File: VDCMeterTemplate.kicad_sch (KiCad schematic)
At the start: 14 parts

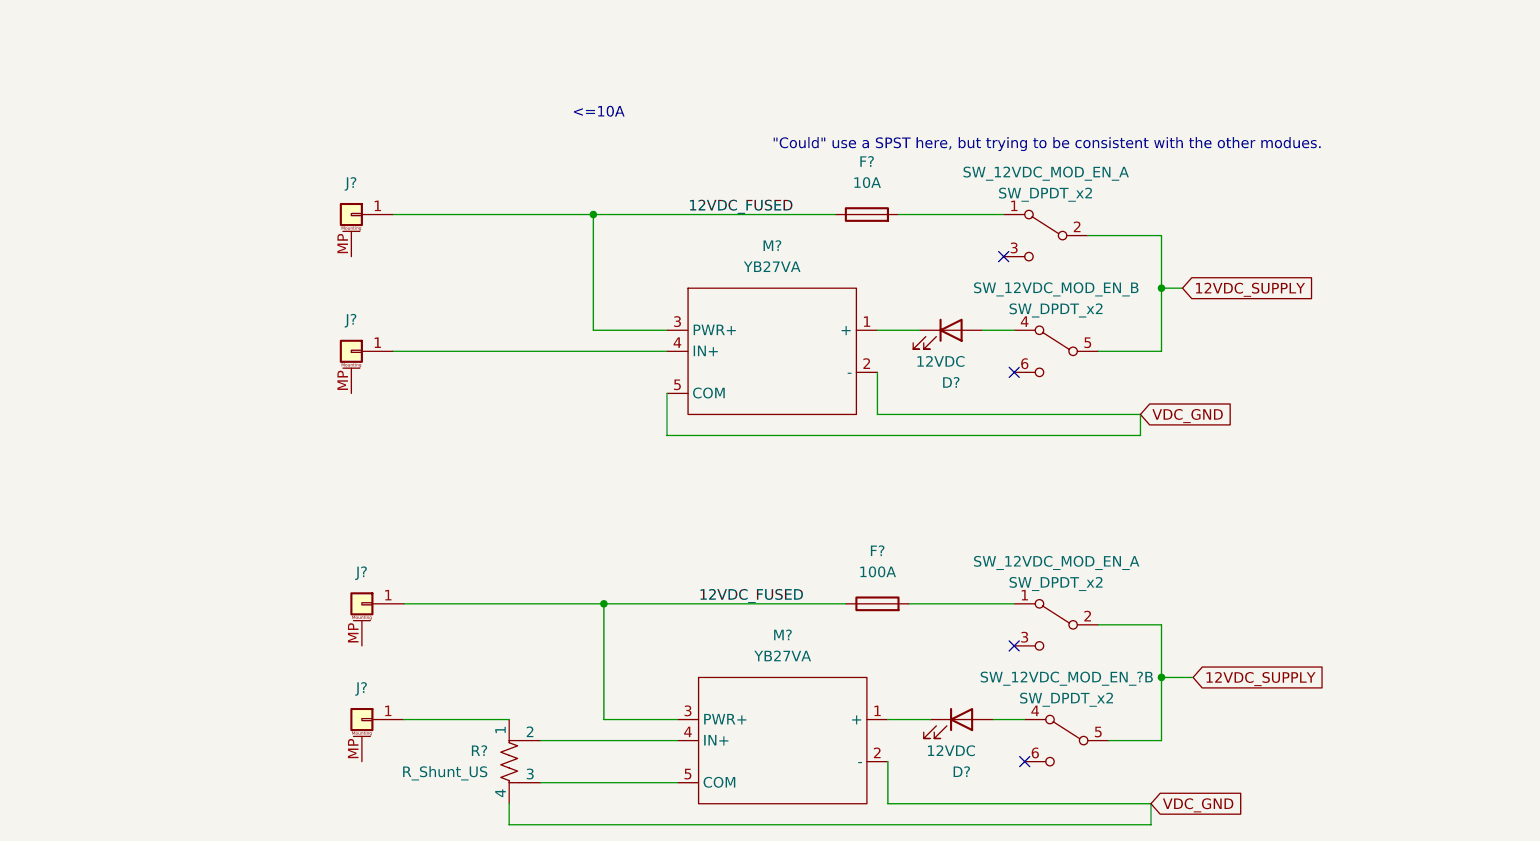
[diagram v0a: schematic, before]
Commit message: Save more changes
Started Fan Control
Created VDC Meter Template
Fleshed out 12, 5, 5-usb, and 3.3 modules
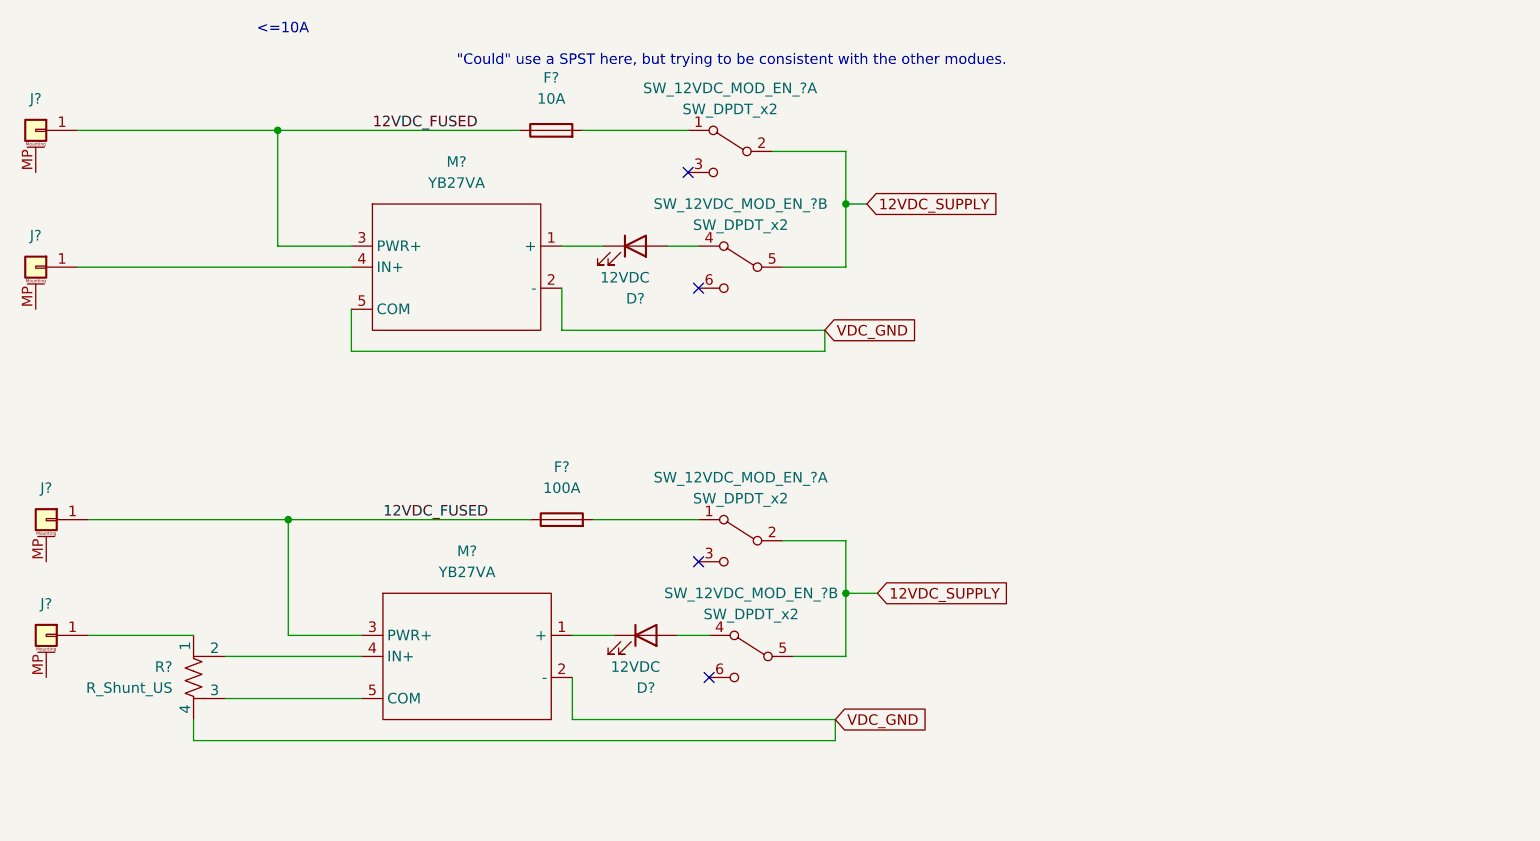
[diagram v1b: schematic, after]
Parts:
- removed D? (x2): 12VDC, symbol Device:LED
- removed F?: 10A, symbol Device:Fuse
- removed F?: 100A, symbol Device:Fuse
- removed J? (x4): Conn_01x01_MountingPin, symbol Connector_Generic_MountingPin:Conn_01x01_MountingPin
- removed M? (x2): YB27VA, symbol bvm-library:5_Pin_Meter_With_Ext_Shunt
- removed R?: R_Shunt_US, symbol Device:R_Shunt_US
- removed SW_12VDC_MOD_EN_ (x2), SW_12VDC_MOD_EN_?: SW_DPDT_x2, symbol Switch:SW_DPDT_x2
- added D? (x2): 12VDC, symbol Device:LED
- added F?: 10A, symbol Device:Fuse
- added F?: 100A, symbol Device:Fuse
- added J? (x4): Conn_01x01_MountingPin, symbol Connector_Generic_MountingPin:Conn_01x01_MountingPin
- added M? (x2): YB27VA, symbol bvm-library:5_Pin_Meter_With_Ext_Shunt
- added R?: R_Shunt_US, symbol Device:R_Shunt_US
- added SW_12VDC_MOD_EN_? (x4): SW_DPDT_x2, symbol Switch:SW_DPDT_x2
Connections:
- net 12VDC_FUSED: now also F?.1, F?.1, J?.1 (Pin_1), J?.1 (Pin_1), M?.3 (PWR+), M?.3 (PWR+)
- net 12VDC_SUPPLY: now also SW_12VDC_MOD_EN_?.2 (B), SW_12VDC_MOD_EN_?.2 (B), SW_12VDC_MOD_EN_?.5 (B), SW_12VDC_MOD_EN_?.5 (B)
- net VDC_GND: now also M?.2 (-), M?.2 (-), M?.5 (COM), R?.4
- new net: F?.2, SW_12VDC_MOD_EN_?.1 (A) (x2)
- new net: J?.1 (Pin_1), R?.1
- new net: M?.4 (IN+), R?.2
- new net: M?.5 (COM), R?.3
- new net: D?.1 (K), M?.1 (+) (x2)
- new net: J?.1 (Pin_1), M?.4 (IN+)
- new net: D?.2 (A), SW_12VDC_MOD_EN_?.4 (A) (x2)
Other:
- company: eatmellc -> (none)

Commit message: Bunch more changes
Blah blah
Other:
- note added: "< 10Amp Version"
- note added: ">= 10Amp Version"
- note added: "Can I make use of some kind of switch that would allow me to enable/disable the shunt?"
- note removed: "<=10A"
- company: (none) -> eatmellc
- title: (none) -> Mr. Powers
- moved on the sheet: D?, F?, J?, M?, SW_12VDC_MOD_EN_?A, SW_12VDC_MOD_EN_?B

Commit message: Minor change across the board
I need better notes.
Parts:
- gave numbers to parts that had none: 13
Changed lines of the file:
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@@
   (symbol (lib_id "Device:Fuse") (at 173.99 38.1 90) (unit 1)
     (in_bom yes) (on_board yes) (fields_autoplaced)
-    (property "Reference" "F?" (id 0) (at 173.99 31.75 90))
+    (property "Reference" "F7" (id 0) (at 173.99 31.75 90))
     (property "Value" "10A" (id 1) (at 173.99 34.29 90))
     (property "Footprint" "" (id 2) (at 173.99 39.878 90)
@@
   (symbol (lib_id "Device:R_Shunt_US") (at 132.08 127 0) (unit 1)
     (in_bom yes) (on_board yes) (fields_autoplaced)
-    (property "Reference" "R?" (id 0) (at 129.54 125.7299 0)
+    (property "Reference" "R5" (id 0) (at 129.54 125.7299 0)
       (effects (font (size 1.27 1.27)) (justify right))
     )
@@
   (symbol (lib_id "Switch:SW_DPDT_x2") (at 198.12 110.49 0) (mirror y) (unit 1)
     (in_bom yes) (on_board yes) (fields_autoplaced)
-    (property "Reference" "SW_12VDC_MOD_EN_?" (id 0) (at 198.12 102.87 0))
+    (property "Reference" "SW_12VDC_MOD_EN_3" (id 0) (at 198.12 102.87 0))
     (property "Value" "SW_DPDT_x2" (id 1) (at 198.12 105.41 0))
     (property "Footprint" "" (id 2) (at 198.12 110.49 0)
@@
   (symbol (lib_id "Connector_Generic_MountingPin:Conn_01x01_MountingPin") (at 114.3 121.92 0) (mirror y) (unit 1)
     (in_bom yes) (on_board yes) (fields_autoplaced)
-    (property "Reference" "J?" (id 0) (at 114.3 118.11 0))
+    (property "Reference" "J19" (id 0) (at 114.3 118.11 0))
     (property "Value" "Conn_01x01_MountingPin" (id 1) (at 111.76 123.5455 0)
       (effects (font (size 1.27 1.27)) (justify left) hide)
@@
   (symbol (lib_id "bvm-library:5_Pin_Meter_With_Ext_Shunt") (at 160.02 127 0) (unit 1)
     (in_bom yes) (on_board yes) (fields_autoplaced)
-    (property "Reference" "M?" (id 0) (at 165.1 111.76 0))
+    (property "Reference" "M11" (id 0) (at 165.1 111.76 0))
     (property "Value" "YB27VA" (id 1) (at 165.1 114.3 0))
     (property "Footprint" "" (id 2) (at 160.02 127 0)
@@
   (symbol (lib_id "Connector_Generic_MountingPin:Conn_01x01_MountingPin") (at 111.76 54.61 0) (mirror y) (unit 1)
     (in_bom yes) (on_board yes) (fields_autoplaced)
-    (property "Reference" "J?" (id 0) (at 111.76 50.8 0))
+    (property "Reference" "J17" (id 0) (at 111.76 50.8 0))
     (property "Value" "Conn_01x01_MountingPin" (id 1) (at 109.22 56.2355 0)
       (effects (font (size 1.27 1.27)) (justify left) hide)
@@
   (symbol (lib_id "Device:LED") (at 184.15 52.07 0) (unit 1)
     (in_bom yes) (on_board yes)
-    (property "Reference" "D?" (id 0) (at 184.15 58.42 0))
+    (property "Reference" "D7" (id 0) (at 184.15 58.42 0))
     (property "Value" "12VDC" (id 1) (at 182.88 55.88 0))
     (property "Footprint" "" (id 2) (at 184.15 52.07 0)
@@
   (symbol (lib_id "Connector_Generic_MountingPin:Conn_01x01_MountingPin") (at 114.3 107.95 0) (mirror y) (unit 1)
     (in_bom yes) (on_board yes) (fields_autoplaced)
-    (property "Reference" "J?" (id 0) (at 114.3 104.14 0))
+    (property "Reference" "J18" (id 0) (at 114.3 104.14 0))
     (property "Value" "Conn_01x01_MountingPin" (id 1) (at 111.76 109.5755 0)
       (effects (font (size 1.27 1.27)) (justify left) hide)
@@
   (symbol (lib_id "bvm-library:5_Pin_Meter_With_Ext_Shunt") (at 157.48 57.15 0) (unit 1)
     (in_bom yes) (on_board yes) (fields_autoplaced)
-    (property "Reference" "M?" (id 0) (at 162.56 41.91 0))
+    (property "Reference" "M10" (id 0) (at 162.56 41.91 0))
     (property "Value" "YB27VA" (id 1) (at 162.56 44.45 0))
     (property "Footprint" "" (id 2) (at 157.48 57.15 0)
@@
   (symbol (lib_id "Device:Fuse") (at 176.53 107.95 90) (unit 1)
     (in_bom yes) (on_board yes) (fields_autoplaced)
-    (property "Reference" "F?" (id 0) (at 176.53 101.6 90))
+    (property "Reference" "F8" (id 0) (at 176.53 101.6 90))
     (property "Value" "100A" (id 1) (at 176.53 104.14 90))
     (property "Footprint" "" (id 2) (at 176.53 109.728 90)
@@
   (symbol (lib_id "Switch:SW_DPDT_x2") (at 195.58 40.64 0) (mirror y) (unit 1)
     (in_bom yes) (on_board yes) (fields_autoplaced)
-    (property "Reference" "SW_12VDC_MOD_EN_?" (id 0) (at 195.58 33.02 0))
+    (property "Reference" "SW_12VDC_MOD_EN_2" (id 0) (at 195.58 33.02 0))
     (property "Value" "SW_DPDT_x2" (id 1) (at 195.58 35.56 0))
     (property "Footprint" "" (id 2) (at 195.58 40.64 0)
@@
   (symbol (lib_id "Switch:SW_DPDT_x2") (at 199.39 124.46 0) (mirror y) (unit 2)
     (in_bom yes) (on_board yes) (fields_autoplaced)
-    (property "Reference" "SW_12VDC_MOD_EN_?" (id 0) (at 199.39 116.84 0))
+    (property "Reference" "SW_12VDC_MOD_EN_3" (id 0) (at 199.39 116.84 0))
     (property "Value" "SW_DPDT_x2" (id 1) (at 199.39 119.38 0))
     (property "Footprint" "" (id 2) (at 199.39 124.46 0)
@@
   (symbol (lib_id "Device:LED") (at 186.69 121.92 0) (unit 1)
     (in_bom yes) (on_board yes)
-    (property "Reference" "D?" (id 0) (at 186.69 128.27 0))
+    (property "Reference" "D8" (id 0) (at 186.69 128.27 0))
     (property "Value" "12VDC" (id 1) (at 185.42 125.73 0))
     (property "Footprint" "" (id 2) (at 186.69 121.92 0)
@@
   (symbol (lib_id "Connector_Generic_MountingPin:Conn_01x01_MountingPin") (at 111.76 38.1 0) (mirror y) (unit 1)
     (in_bom yes) (on_board yes) (fields_autoplaced)
-    (property "Reference" "J?" (id 0) (at 111.76 34.29 0))
+    (property "Reference" "J16" (id 0) (at 111.76 34.29 0))
     (property "Value" "Conn_01x01_MountingPin" (id 1) (at 109.22 39.7255 0)
       (effects (font (size 1.27 1.27)) (justify left) hide)
@@
   (symbol (lib_id "Switch:SW_DPDT_x2") (at 196.85 54.61 0) (mirror y) (unit 2)
     (in_bom yes) (on_board yes) (fields_autoplaced)
-    (property "Reference" "SW_12VDC_MOD_EN_?" (id 0) (at 196.85 46.99 0))
+    (property "Reference" "SW_12VDC_MOD_EN_2" (id 0) (at 196.85 46.99 0))
     (property "Value" "SW_DPDT_x2" (id 1) (at 196.85 49.53 0))
     (property "Footprint" "" (id 2) (at 196.85 54.61 0)
